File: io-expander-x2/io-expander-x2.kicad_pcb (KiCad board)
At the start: 2 copper layers, 50 x 100 mm, 17 parts, among them IC1 MCP23017-E_SO, IC2 MCP23017-E_SO, J1 CONN4_BM04B-SRSS_JST, J2 CONN4_BM04B-SRSS_JST, J3 8 Position Screw Terminal, J4 8 Position Screw Terminal, J5 8 Position Screw Terminal, J6 8 Position Screw Terminal

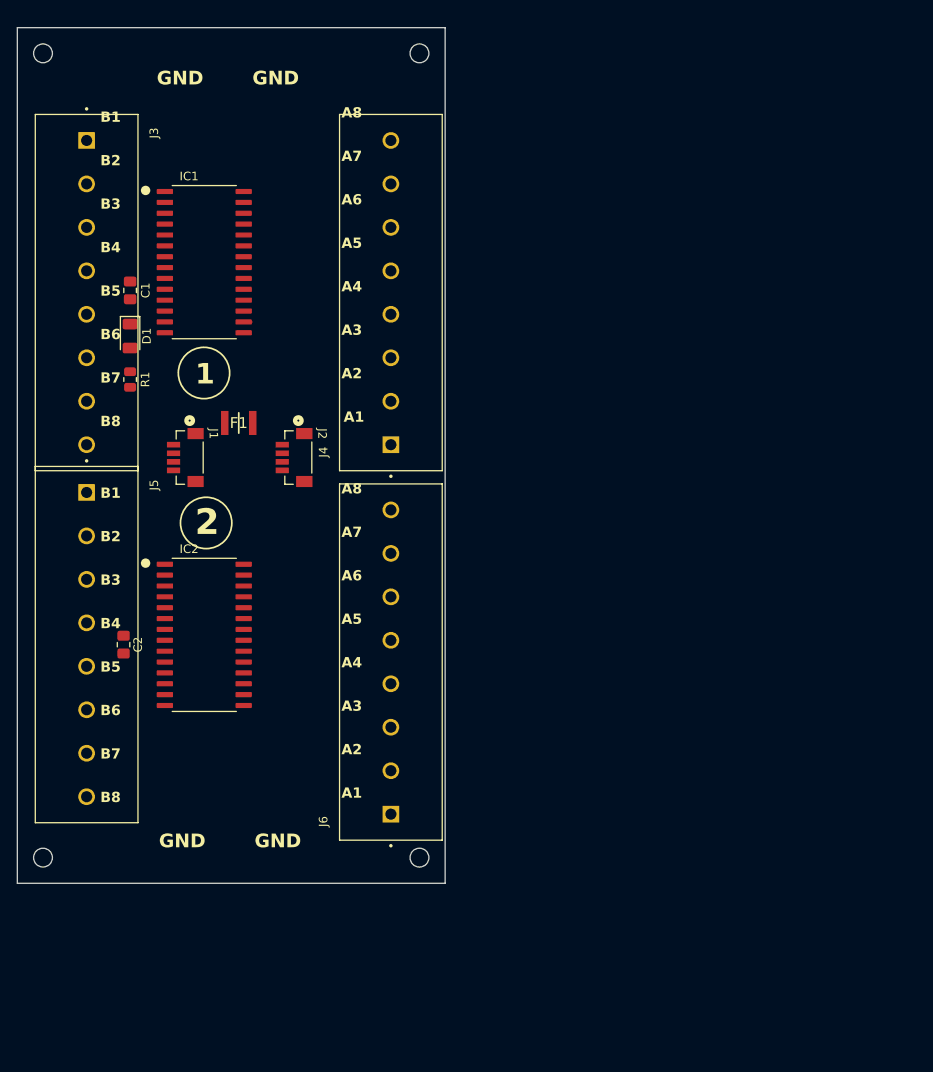
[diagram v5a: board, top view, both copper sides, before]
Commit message: Board is larger. Rotated 90 degrees. New connector types selected.
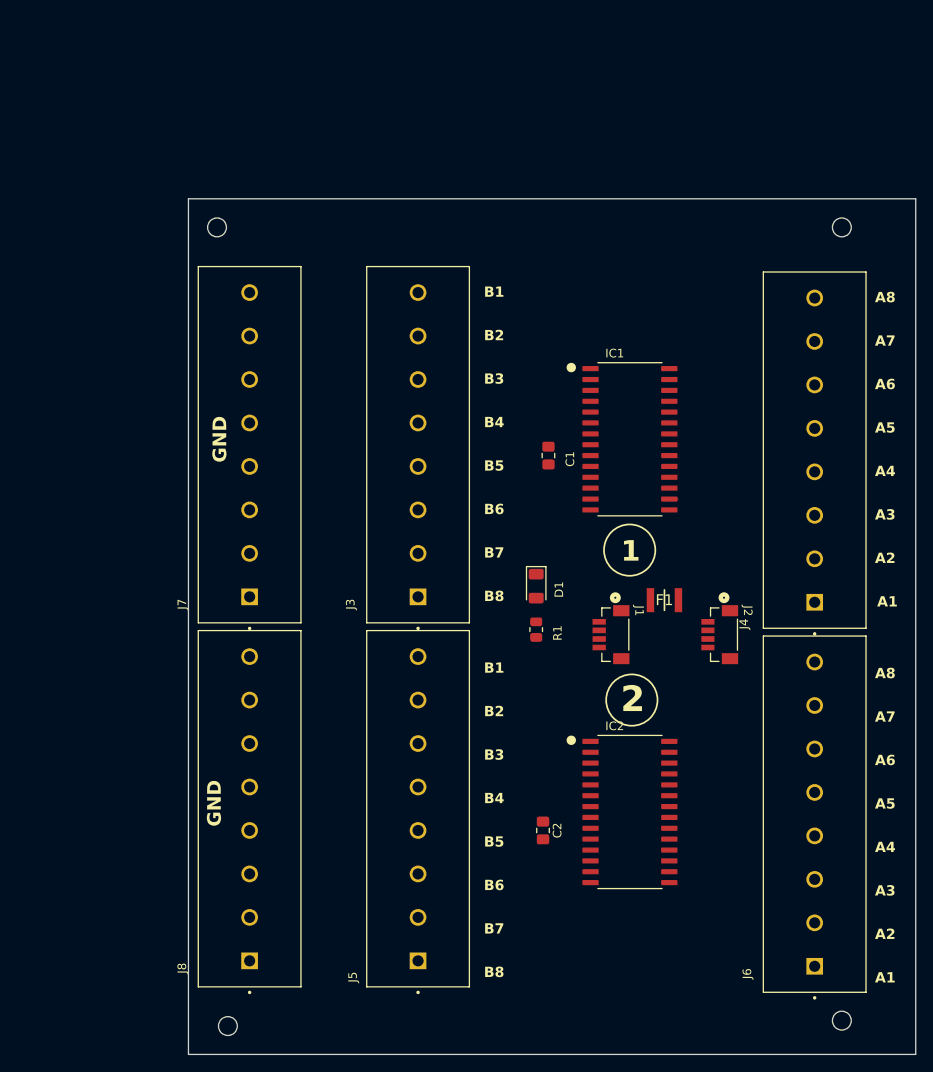
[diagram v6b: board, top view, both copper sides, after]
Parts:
- added J7: 8 Position Screw Terminal, 00_connectors:PHOENIX_1869279, F.Cu at (63.1, 99.6)
- added J8: 8 Position Screw Terminal, 00_connectors:PHOENIX_1869279, F.Cu at (63.1, 142.1)
- J1, J2: value CONN4_BM04B-SRSS_JST -> QWIIC
- moved J5 79.2 mm to (82.8, 142.1), turned to 90 degrees
- moved J3 78.1 mm to (82.8, 99.6), turned to 90 degrees
- moved D1 55.7 mm to (90.6, 95.3)
- moved R1 55.7 mm to (90.6, 100.4)
- moved J1 53.9 mm to (99.9, 100.9)
- moved F1 53.9 mm to (105.6, 96.9)
- moved IC1 53.9 mm to (101.6, 78.1)
- moved IC2 53.9 mm to (101.6, 121.7)
- moved J2 53.9 mm to (112.6, 100.9)
- moved C2 53.6 mm to (91.4, 123.8)
- moved H2 53.4 mm to (126.4, 53.3)
- moved H4 52.9 mm to (126.4, 146.1)
- moved J4 52.8 mm to (129.2, 100.2)
- moved J6 52.6 mm to (129.2, 142.7)
- moved C1 52.6 mm to (92.1, 80.0)
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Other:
- board size 50 x 100 mm -> 85 x 100 mm
